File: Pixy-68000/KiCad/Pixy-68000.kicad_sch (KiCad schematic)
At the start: 94 parts, among them J1 AVR_ISP, J11 USB, J4 Socket5, J5 Socket5, J6 JTAG, J6 Socket5, J7 Socket5, SW0 SW0, SW1 SW1, SW2 SW2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

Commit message: Completed artwork 68000-0.
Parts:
- removed D14: LED7, kekyo:LED_D3.0mm, symbol Device:LED
- removed D14: LED5, kekyo:LED_D3.0mm, symbol Device:LED
- removed D14: LED4, kekyo:LED_D3.0mm, symbol Device:LED
- removed D14: LED6, kekyo:LED_D3.0mm, symbol Device:LED
- removed D14: ACC, kekyo:LED_D3.0mm, symbol Device:LED
- removed R17 (x5): 2k, kekyo:R_0805_2012, symbol Device:R
- added C11: 0.1u, kekyo:C_0805_2012, symbol kekyo:C
- added D14: HALT, kekyo:LED_D3.0mm, symbol Device:LED
- added J10: Header3, kekyo:PinHeader_1x03_P2.54mm_Vertical, symbol kekyo:Header3
- added J8: BUS, Connector_PinHeader_2.54mm:PinHeader_2x25_P2.54mm_Vertical, symbol kekyo:Conn_02x25_Odd_Even
- added J9: Header8, kekyo:PinHeader_1x08_P2.54mm_Vertical, symbol kekyo:Header8
- added R17: 2k, kekyo:R_0805_2012, symbol Device:R
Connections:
- net ACC is gone; now on net /OE: U4.36 (PB10A)
- net BD0 is gone; now on net D0: U10.13 (D0)
- net BD1 is gone; now on net D1: U10.14 (D1)
- net BD10 is gone; now on net D10: U11.15 (D2)
- net BD11 is gone; now on net D11: U11.17 (D3)
- net BD12 is gone; now on net D12: U11.18 (D4)
- net BD13 is gone; now on net D13: U11.19 (D5)
- net BD14 is gone; now on net D14: U11.20 (D6)
- net BD15 is gone; now on net D15: U11.21 (D7)
- net BD2 is gone; now on net D2: U10.15 (D2)
- net BD3 is gone; now on net D3: U10.17 (D3)
- net BD4 is gone; now on net D4: U10.18 (D4)
- net BD5 is gone; now on net D5: U10.19 (D5)
- net BD6 is gone; now on net D6: U10.20 (D6)
- net BD7 is gone; now on net D7: U10.21 (D7)
- net BD8 is gone; now on net D8: U11.13 (D0)
- net BD9 is gone; now on net D9: U11.14 (D1)
- net LED4 is gone; now on net LED0: U5.27 (PC4)
- net LED5 is gone; now on net LED1: U5.28 (PC5)
- net LED6 is gone; now on net LED2: U5.2 (PD4)
- net LED7 is gone; now on net LED3: U5.9 (PD5)
- net /WE is gone; now on net R/W: U10.31 (PGM), U11.31 (PGM), U6.15 (~{WE}), U7.15 (~{WE})
- net A0: now also J8.2 (Pin_2)
- net A1: now also J8.4 (Pin_4)
- net A10: now also J8.22 (Pin_22)
- net A11: now also J8.24 (Pin_24)
- net A12: now also J8.26 (Pin_26)
- net A13: now also J8.28 (Pin_28)
- net A14: now also J8.30 (Pin_30)
- net A15: now also J8.32 (Pin_32)
- net A16: now also J8.34 (Pin_34)
- net A17: now also J8.36 (Pin_36)
- net A18: now also J8.38 (Pin_38)
- net A19: now also J8.40 (Pin_40)
- net A2: now also J8.6 (Pin_6)
- net A20: now also J8.42 (Pin_42)
- net A21: now also J8.44 (Pin_44)
- net A22: now also J8.46 (Pin_46)
- net A23: now also J8.48 (Pin_48)
- net A3: now also J8.8 (Pin_8)
- net A4: now also J8.10 (Pin_10)
- net A5: now also J8.12 (Pin_12)
- net A6: now also J8.14 (Pin_14)
- net A7: now also J8.16 (Pin_16)
- net A8: now also J8.18 (Pin_18)
- net A9: now also J8.20 (Pin_20)
- net CPUCLK: now also J10.1 (P0)
- net D0: now also J8.1 (Pin_1)
- net D1: now also J8.3 (Pin_3)
- net D10: now also J8.21 (Pin_21)
- net D11: now also J8.23 (Pin_23)
- net D12: now also J8.25 (Pin_25)
- net D13: now also J8.27 (Pin_27)
- net D14: now also J8.29 (Pin_29)
- net D15: now also J8.31 (Pin_31)
- net D2: now also J8.5 (Pin_5)
- net D3: now also J8.7 (Pin_7)
- net D4: now also J8.9 (Pin_9)
- net D5: now also J8.11 (Pin_11)
- net D6: now also J8.13 (Pin_13)
- net D7: now also J8.15 (Pin_15)
- net D8: now also J8.17 (Pin_17)
- net D9: now also J8.19 (Pin_19)
- net FC0: now also J8.43 (Pin_43)
- net FC1: now also J8.45 (Pin_45)
- net FC2: now also J8.47 (Pin_47)
- net GND: now also C11.2, J10.2 (P1), J10.3 (P2), J9.3 (P2), J9.4 (P3), J9.5 (P4), J9.6 (P5), J9.7 (P6), J9.8 (P7)
- net LED0: no longer U5.23 (PC0)
- net LED1: no longer U5.24 (PC1)
- net LED2: no longer U5.25 (PC2)
- net LED3: no longer U5.26 (PC3)
- net LEDDIO0: now also U5.23 (PC0); no longer U4.27 (PB4A/CSSPIN)
- net LEDDIO1: now also U5.24 (PC1); no longer U4.28 (PB4B)
- net LEDRCK: now also U5.26 (PC3); no longer U4.30 (PB4D)
- net LEDSCK: now also U5.25 (PC2); no longer U4.29 (PB4C)
- net R/W: now also J8.39 (Pin_39)
- net VCC: now also C11.1, J9.1 (P0), J9.2 (P1), R17.1
- net /AS: now also J8.33 (Pin_33)
- net /AVEC: now also J8.49 (Pin_49)
- net /DTACK: now also J8.41 (Pin_41)
- net /HALT: now also D14.1 (K)
- net /IPL0: now also J8.50 (Pin_50)
- net /LDS: now also J8.37 (Pin_37)
- net /PROMCS0: now also U4.29 (PB4C)
- net /PROMCS1: now also U4.30 (PB4D)
- net /SRAMCS0: now also U4.27 (PB4A/CSSPIN)
- net /SRAMCS1: now also U4.28 (PB4B)
- net /UDS: now also J8.35 (Pin_35)
- new net: D14.2 (A), R17.2
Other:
- moved on the sheet: D14, R17

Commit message: Refactored directory structure.
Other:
- company: (none) -> (c) Kouji Matsui
- title: (none) -> Pixy-68000-0
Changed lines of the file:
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@@
 (kicad_sch (version 20230121) (generator eeschema)
   (paper "A2")
+  (title_block
+    (title "Pixy-68000-0")
+    (date "2023-11-25")
+    (rev "0")
+    (company "(c) Kouji Matsui")
+    (comment 1 "https://github.com/kekyo/Pixy")
+  )
   (junction (at 388.62 96.52) (diameter 0) (color 0 0 0 0)
   )

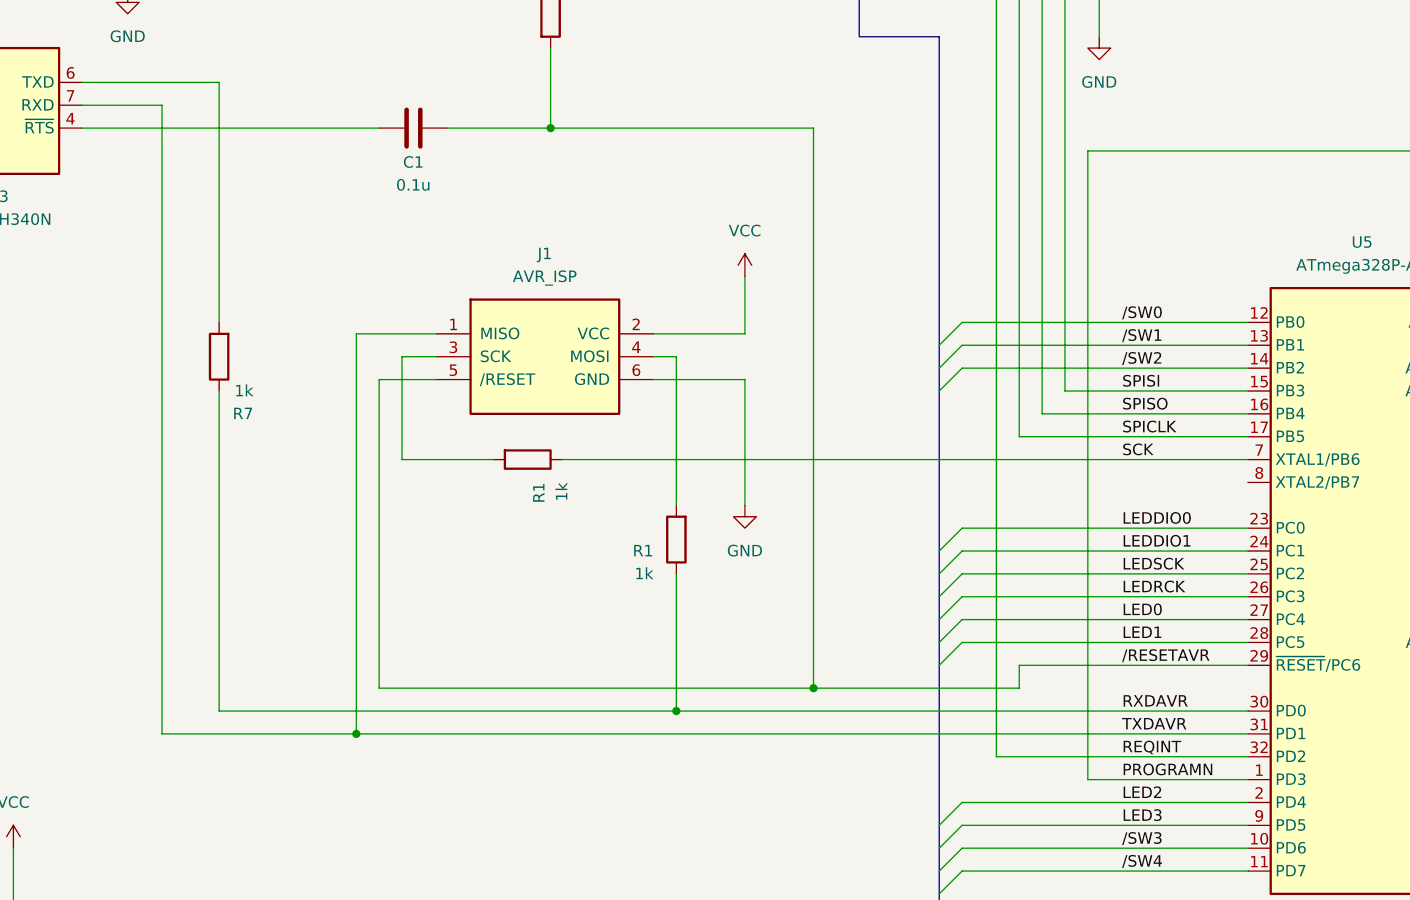
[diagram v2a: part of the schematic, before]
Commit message: Fixed bootloading JTAG signal lines on ATMega328P.
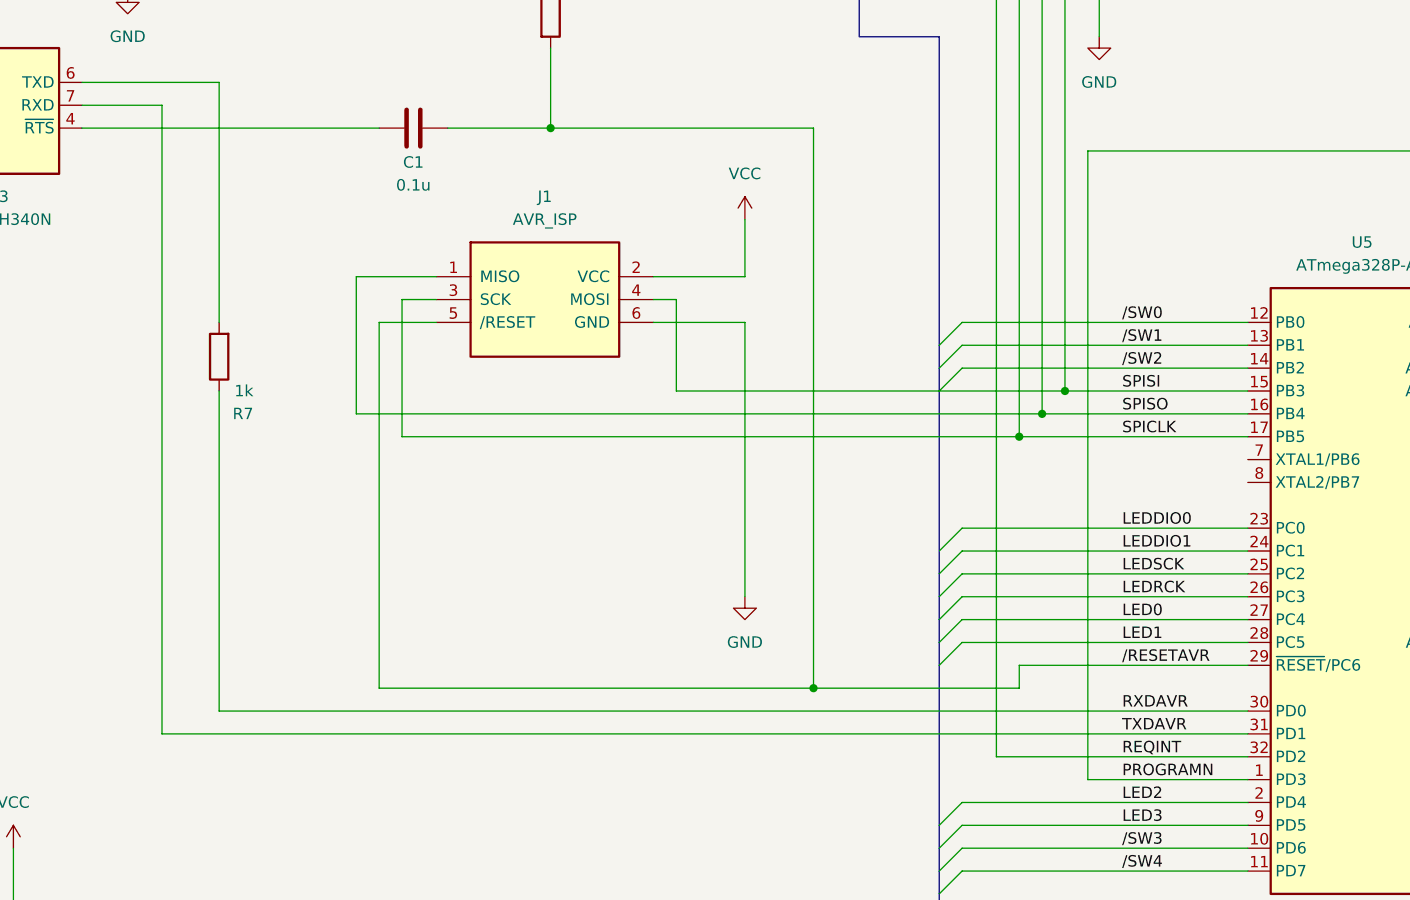
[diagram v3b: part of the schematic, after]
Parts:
- removed R1 (x2): 1k, kekyo:R_0805_2012, symbol kekyo:R
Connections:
- net SPICLK: now also J1.3 (SCK)
- net SPISI: now also J1.4 (MOSI)
- net SPISO: now also J1.1 (MISO)
- net TXDAVR: no longer J1.1 (MISO)
- net SCK: no longer names the net of U5.7 (XTAL1/PB6)
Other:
- moved on the sheet: J1

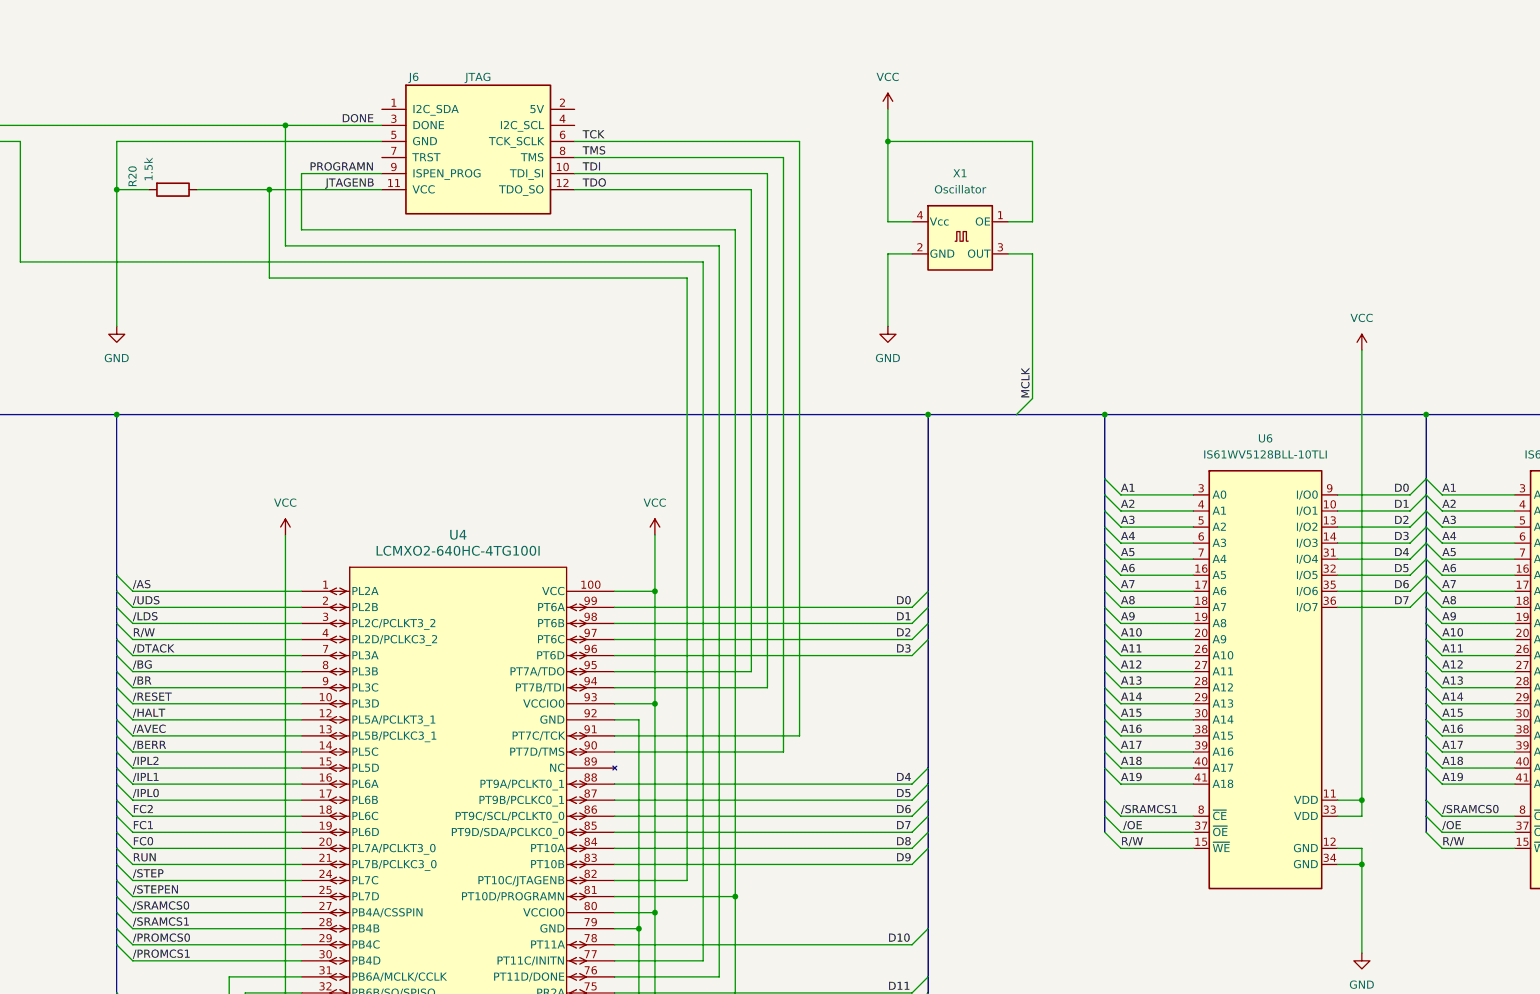
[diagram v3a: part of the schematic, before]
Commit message: Fixed JTAG pin header assignment.
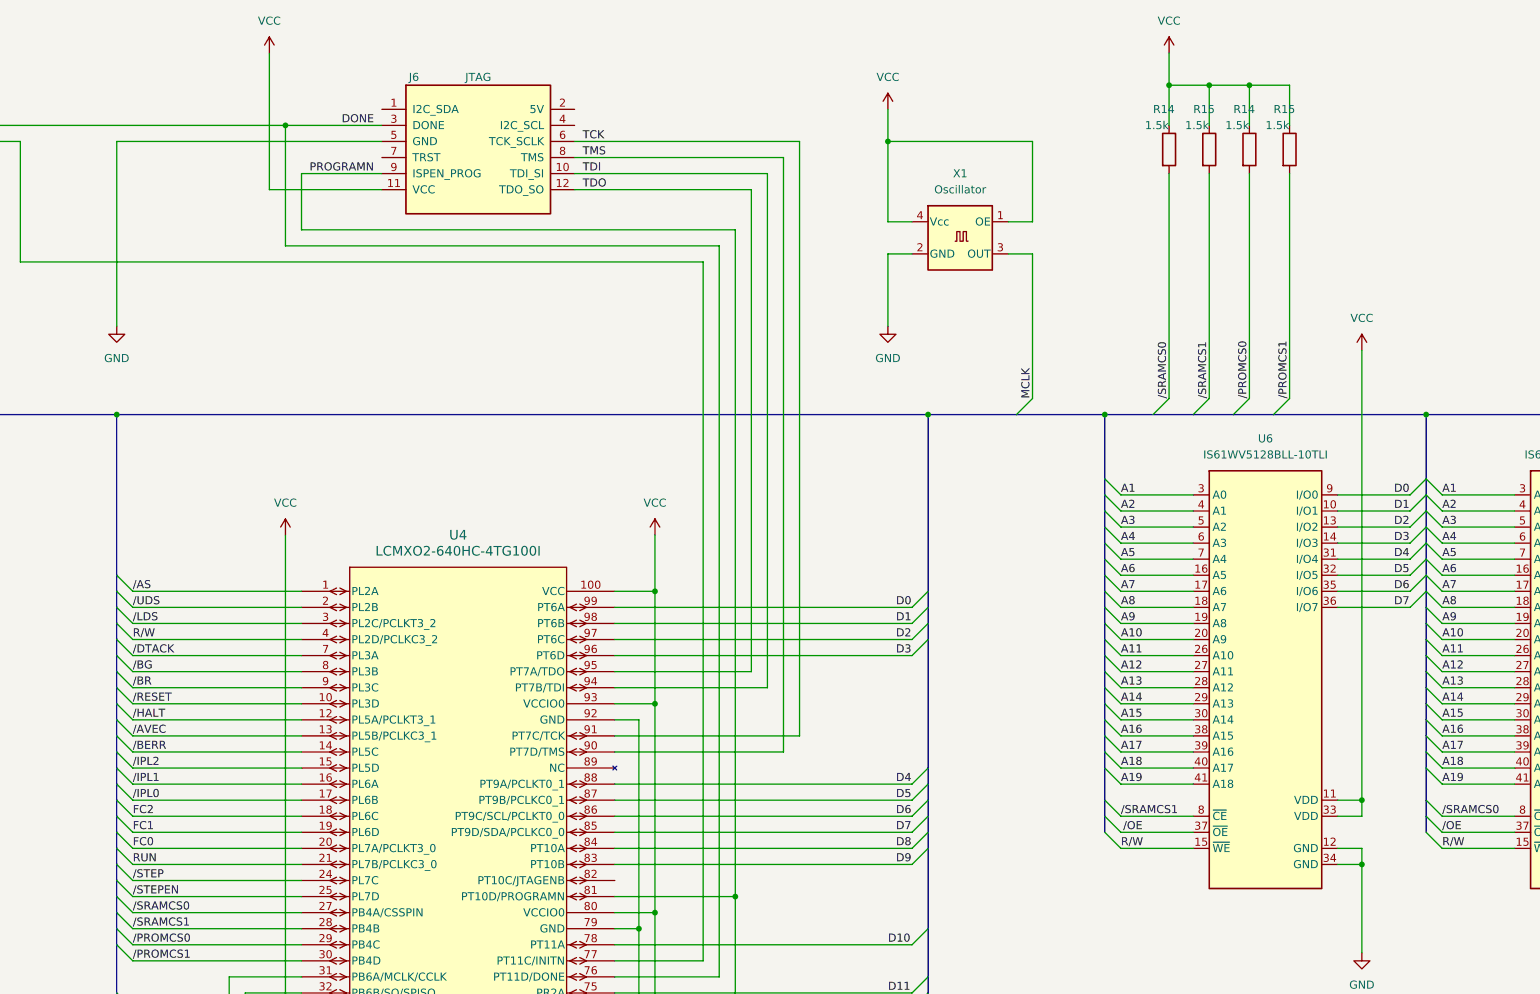
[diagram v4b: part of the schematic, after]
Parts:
- removed R20: 1.5k, kekyo:R_0805_2012, symbol Device:R
- added R14 (x2), R15 (x2): 1.5k, kekyo:R_0805_2012, symbol Device:R
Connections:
- net VCC: now also J6.11 (VCC), R14.1, R14.1, R15.1, R15.1
- net /PROMCS0: now also R14.2
- net /PROMCS1: now also R15.2
- net /SRAMCS0: now also R14.2
- net /SRAMCS1: now also R15.2
- net JTAGENB: no longer names the net of U4.82 (PT10C/JTAGENB)
- net JTAGENB: no longer J6.11 (VCC)

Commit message: Refactored.
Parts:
- removed R7: 1k, kekyo:R_0805_2012, symbol kekyo:R
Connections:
- net RXDAVR: now also U3.6 (TXD)
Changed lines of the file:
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@@
     (stroke (width 0) (type default))
   )
-  (wire (pts (xy 110.49 302.26) (xy 110.49 337.82))
-    (stroke (width 0) (type default))
-  )
   (wire (pts (xy 287.02 55.88) (xy 287.02 149.86))
     (stroke (width 0) (type default))
@@
     (stroke (width 0) (type default))
   )
-  (wire (pts (xy 110.49 267.97) (xy 110.49 294.64))
+  (wire (pts (xy 110.49 267.97) (xy 110.49 337.82))
     (stroke (width 0) (type default))
   )
@@
         )
       )
-    )
-  )
-  (symbol (lib_id "kekyo:R") (at 110.49 298.45 180) (unit 1)
-    (in_bom yes) (on_board yes) (dnp no)
-    (property "Reference" "R7" (at 114.3 304.8 0)
-      (effects (font (size 1.27 1.27)) (justify left))
-    )
-    (property "Value" "1k" (at 114.3 302.26 0)
-      (effects (font (size 1.27 1.27)) (justify left))
-    )
-    (property "Footprint" "kekyo:R_0805_2012" (at 112.268 298.45 90)
-      (effects (font (size 1.27 1.27)) hide)
-    )
-    (property "Datasheet" "~" (at 110.49 298.45 0)
-      (effects (font (size 1.27 1.27)) hide)
-    )
-    (pin "1")
-    (pin "2")
-    (instances
-      (project "Pixy-mega128"
-        (path "/7609de31-cb73-4ace-8f34-65caa63c74e9"
-          (reference "R7") (unit 1)
-        )
-      )
-      (project "MC68SEC000"
-        (path "/7907391b-035a-42ea-89b1-82b781ee98c8"
-          (reference "R20") (unit 1)
-        )
-      )
-      (project "Pixy-68000"
-        (path "/9aeb2b9d-08f7-44b5-9289-68c429469433"
-          (reference "R7") (unit 1)
-        )
-      )

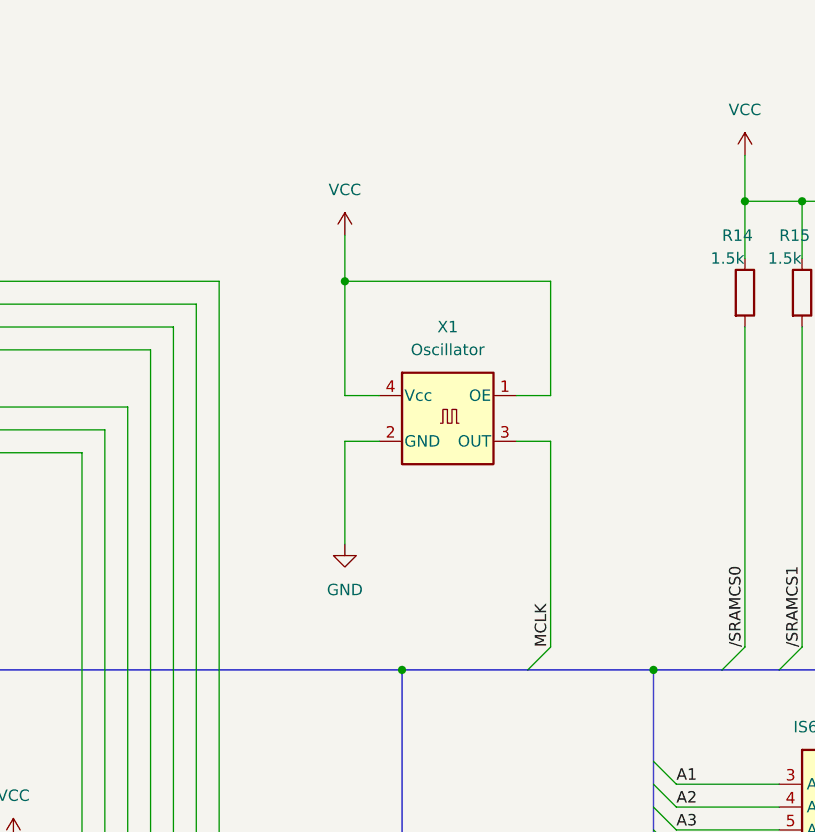
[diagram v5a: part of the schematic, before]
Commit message: Improved JTAG stability.
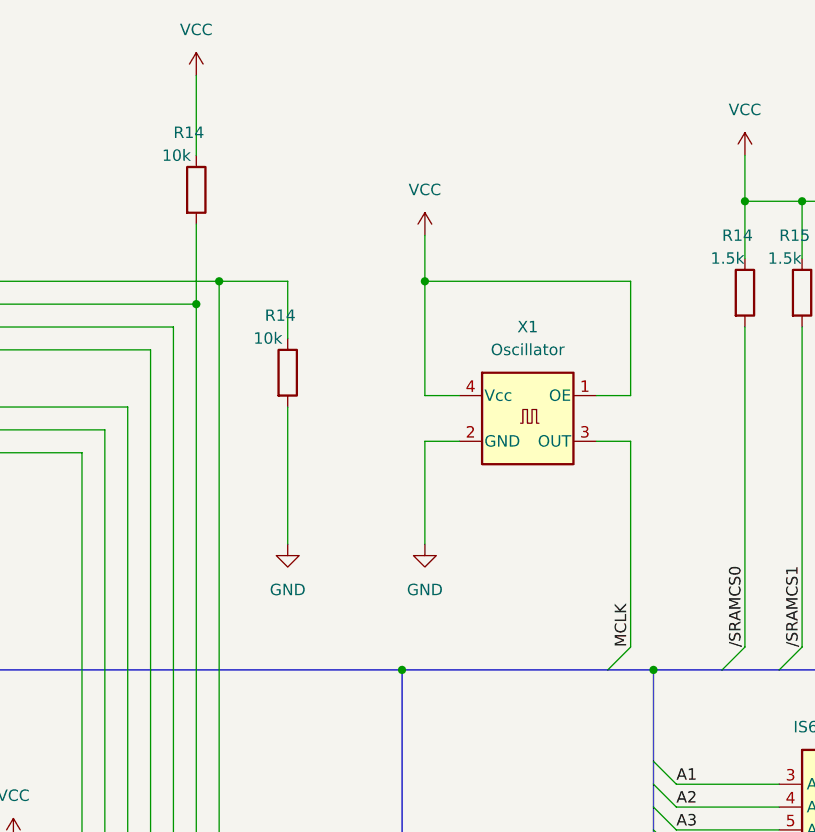
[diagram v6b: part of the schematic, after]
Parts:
- added R14 (x2): 10k, kekyo:R_0805_2012, symbol Device:R
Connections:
- net GND: now also R14.2
- net TCK: now also R14.1
- net TMS: now also R14.2
- net VCC: now also R14.1
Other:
- moved on the sheet: X1
